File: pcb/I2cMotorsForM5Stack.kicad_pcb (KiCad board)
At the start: 2 copper layers, 60 x 50 mm, 34 parts, among them J1 FFC_connector, J2 2x15socket, J3 Conn_01x06, J4 Conn_01x06, J5 Conn_01x04, U1 TB6612FNG, U2 ATmega328PB-MU

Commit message: Rename project to I2cMotorsForM5Stack
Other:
- board text added: "I2cMotorsForM5Stack"
- board text removed: "I2CMotorsForM5Stack"
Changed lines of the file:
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@@
     (effects (font (size 1 1) (thickness 0.15)))
   )
-  (gr_text I2CMotorsForM5Stack (at 126.2988 98.5832) (layer F.SilkS)
+  (gr_text I2cMotorsForM5Stack (at 126.2988 98.5832) (layer F.SilkS)
     (effects (font (size 1.3 1.3) (thickness 0.325)))
   )
@@
     (effects (font (size 1 1) (thickness 0.15)) (justify mirror))
   )
-  (gr_text I2CMotorsForM5Stack (at 125.6988 96.5332) (layer B.SilkS)
+  (gr_text I2cMotorsForM5Stack (at 125.6988 96.5332) (layer B.SilkS)
     (effects (font (size 1.3 1.3) (thickness 0.325)) (justify mirror))
   )

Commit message: Add explanation about pads to configure address
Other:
- board text added: "Default: 0b01010010 = 0x52 = 82"
- board text added: "Pads to configure I2C slave address."
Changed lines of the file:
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@@
   (general
     (thickness 1.6)
-    (drawings 38)
+    (drawings 40)
     (tracks 593)
     (zones 0)
@@
     )
     (pad 1 np_thru_hole circle (at 0 0) (size 2.2 2.2) (drill 2.2) (layers *.Cu *.Mask))
+  )
+  (gr_text "Default: 0b01010010 = 0x52 = 82" (at 121.4238 84.6332) (layer B.SilkS)
+    (effects (font (size 1 1) (thickness 0.15)) (justify mirror))
+  )
+  (gr_text "Pads to configure I2C slave address." (at 120.8738 82.4582) (layer B.SilkS)
+    (effects (font (size 1 1) (thickness 0.15)) (justify mirror))
   )
   (gr_text GND (at 130.7488 58.2082 270) (layer F.SilkS)
@@
   (segment (start 115.1587 81.7405) (end 116.0785 80.8207) (width 0.25) (layer F.Cu) (net 46))
   (segment (start 116.0785 80.8207) (end 120.161 80.8207) (width 0.25) (layer F.Cu) (net 46))
-  (segment (start 117.9504 85.5915) (end 117.6452 85.8967) (width 0.25) (layer B.Cu) (net 58))
-  (segment (start 119.4735 84.5082) (end 118.9851 84.5082) (width 0.25) (layer F.Cu) (net 58))
-  (segment (start 118.9851 84.5082) (end 117.9504 85.5429) (width 0.25) (layer F.Cu) (net 58))
-  (segment (start 117.9504 85.5429) (end 117.9504 85.5915) (width 0.25) (layer F.Cu) (net 58))
-  (via (at 117.9504 85.5915) (size 0.8) (layers F.Cu B.Cu) (net 58))
-  (segment (start 116.4238 87.1181) (end 117.9504 85.5915) (width 0.25) (layer B.Cu) (net 58))
-  (segment (start 116.4238 92.5582) (end 116.4238 87.1181) (width 0.25) (layer B.Cu) (net 58))
   (via (at 118.1488 86.6832) (size 0.8) (drill 0.4) (layers F.Cu B.Cu) (net 47))
   (segment (start 119.4735 85.0082) (end 119.4735 85.3585) (width 0.25) (layer F.Cu) (net 47))
@@
   (segment (start 118.1488 91.7332) (end 118.9738 92.5582) (width 0.25) (layer B.Cu) (net 47))
   (segment (start 118.1488 86.6832) (end 118.1488 91.7332) (width 0.25) (layer B.Cu) (net 47))
-  (segment (start 94.4988 62.0082) (end 94.0488 62.4582) (width 1) (layer F.Cu) (net 49))
-  (segment (start 105.299 62.0082) (end 94.4988 62.0082) (width 1) (layer F.Cu) (net 49))
   (segment (start 120.161 85.6957) (end 120.0653 85.6957) (width 0.25) (layer F.Cu) (net 48))
   (segment (start 120.0653 85.6957) (end 118.8851 86.8759) (width 0.25) (layer F.Cu) (net 48))
@@
   (segment (start 121.5238 91.6079) (end 118.8851 88.9692) (width 0.25) (layer B.Cu) (net 48))
   (segment (start 121.5238 92.5582) (end 121.5238 91.6079) (width 0.25) (layer B.Cu) (net 48))
+  (segment (start 94.4988 62.0082) (end 94.0488 62.4582) (width 1) (layer F.Cu) (net 49))
+  (segment (start 105.299 62.0082) (end 94.4988 62.0082) (width 1) (layer F.Cu) (net 49))
   (segment (start 120.661 85.6957) (end 120.661 86.1841) (width 0.25) (layer F.Cu) (net 50))
   (segment (start 120.661 86.1841) (end 120.3864 86.4587) (width 0.25) (layer F.Cu) (net 50))
@@
   (segment (start 110.9485 70.568898) (end 110.02379 71.493608) (width 1) (layer F.Cu) (net 57))
   (segment (start 111.124 76.5582) (end 113.6488 76.5582) (width 1) (layer F.Cu) (net 57))
+  (segment (start 117.9504 85.5915) (end 117.6452 85.8967) (width 0.25) (layer B.Cu) (net 58))
+  (segment (start 119.4735 84.5082) (end 118.9851 84.5082) (width 0.25) (layer F.Cu) (net 58))
+  (segment (start 118.9851 84.5082) (end 117.9504 85.5429) (width 0.25) (layer F.Cu) (net 58))
+  (segment (start 117.9504 85.5429) (end 117.9504 85.5915) (width 0.25) (layer F.Cu) (net 58))
+  (via (at 117.9504 85.5915) (size 0.8) (layers F.Cu B.Cu) (net 58))
+  (segment (start 116.4238 87.1181) (end 117.9504 85.5915) (width 0.25) (layer B.Cu) (net 58))
+  (segment (start 116.4238 92.5582) (end 116.4238 87.1181) (width 0.25) (layer B.Cu) (net 58))
   (zone (net 1) (net_name GND) (layer F.Cu) (hatch edge 0.508)
     (connect_pads (clearance 0.508))

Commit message: Update something
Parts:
- removed JP3, JP4: NO, Jumper:SolderJumper-2_P1.3mm_Open_RoundedPad1.0x1.5mm
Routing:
- net Net-(JP3-Pad2): track 4.54 -> 0.00 mm
- net Net-(JP4-Pad2): track 4.42 -> 0.00 mm
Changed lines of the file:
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@@
     (thickness 1.6)
     (drawings 40)
-    (tracks 593)
+    (tracks 588)
     (zones 0)
-    (modules 34)
+    (modules 32)
     (nets 59)
   )
@@
       (rotate (xyz 0 0 0))
     )
-  )
-  (module Jumper:SolderJumper-2_P1.3mm_Open_RoundedPad1.0x1.5mm (layer F.Cu)
-    (at 128.924 81.3082 180)
-    (descr "SMD Solder Jumper, 1x1.5mm, rounded Pads, 0.3mm gap, open")
-    (tags "solder jumper open")
-    (attr virtual)
-    (fp_text reference JP4 (at 0 -1.8) (layer F.SilkS) hide
-      (effects (font (size 1 1) (thickness 0.15)))
-    )
-    (fp_text value NO (at 0 1.9) (layer F.Fab)
-      (effects (font (size 1 1) (thickness 0.15)))
-    )
-    (fp_line (start 1.65 1.25) (end -1.65 1.25) (layer F.CrtYd) (width 0.05))
-    (fp_line (start 1.65 1.25) (end 1.65 -1.25) (layer F.CrtYd) (width 0.05))
-    (fp_line (start -1.65 -1.25) (end -1.65 1.25) (layer F.CrtYd) (width 0.05))
-    (fp_line (start -1.65 -1.25) (end 1.65 -1.25) (layer F.CrtYd) (width 0.05))
-    (fp_line (start -0.7 -1) (end 0.7 -1) (layer F.SilkS) (width 0.12))
-    (fp_line (start 1.4 -0.3) (end 1.4 0.3) (layer F.SilkS) (width 0.12))
-    (fp_line (start 0.7 1) (end -0.7 1) (layer F.SilkS) (width 0.12))
-    (fp_line (start -1.4 0.3) (end -1.4 -0.3) (layer F.SilkS) (width 0.12))
-    (fp_arc (start -0.7 -0.3) (end -0.7 -1) (angle -90) (layer F.SilkS) (width 0.12))
-    (fp_arc (start -0.7 0.3) (end -1.4 0.3) (angle -90) (layer F.SilkS) (width 0.12))
-    (fp_arc (start 0.7 0.3) (end 0.7 1) (angle -90) (layer F.SilkS) (width 0.12))
-    (fp_arc (start 0.7 -0.3) (end 1.4 -0.3) (angle -90) (layer F.SilkS) (width 0.12))
-    (pad 2 smd custom (at 0.65 0 180) (size 1 0.5) (layers F.Cu F.Mask)
-      (net 56 "Net-(JP4-Pad2)") (zone_connect 2)
-      (options (clearance outline) (anchor rect))
-      (primitives
-        (gr_circle (center 0 0.25) (end 0.5 0.25) (width 0))
-        (gr_circle (center 0 -0.25) (end 0.5 -0.25) (width 0))
-        (gr_poly (pts
-           (xy 0 -0.75) (xy -0.5 -0.75) (xy -0.5 0.75) (xy 0 0.75)) (width 0))
-      ))
-    (pad 1 smd custom (at -0.65 0 180) (size 1 0.5) (layers F.Cu F.Mask)
-      (net 4 +3V3) (zone_connect 2)
-      (options (clearance outline) (anchor rect))
-      (primitives
-        (gr_circle (center 0 0.25) (end 0.5 0.25) (width 0))
-        (gr_circle (center 0 -0.25) (end 0.5 -0.25) (width 0))
-        (gr_poly (pts
-           (xy 0 -0.75) (xy 0.5 -0.75) (xy 0.5 0.75) (xy 0 0.75)) (width 0))
-      ))
-  )
-  (module Jumper:SolderJumper-2_P1.3mm_Open_RoundedPad1.0x1.5mm (layer F.Cu)
-    (at 128.924 85.4832 180)
-    (descr "SMD Solder Jumper, 1x1.5mm, rounded Pads, 0.3mm gap, open")
-    (tags "solder jumper open")
-    (attr virtual)
-    (fp_text reference JP3 (at 0 -1.8) (layer F.SilkS) hide
-      (effects (font (size 1 1) (thickness 0.15)))
-    )
-    (fp_text value NO (at 0 1.9) (layer F.Fab)
-      (effects (font (size 1 1) (thickness 0.15)))
-    )
-    (fp_line (start 1.65 1.25) (end -1.65 1.25) (layer F.CrtYd) (width 0.05))
-    (fp_line (start 1.65 1.25) (end 1.65 -1.25) (layer F.CrtYd) (width 0.05))
-    (fp_line (start -1.65 -1.25) (end -1.65 1.25) (layer F.CrtYd) (width 0.05))
-    (fp_line (start -1.65 -1.25) (end 1.65 -1.25) (layer F.CrtYd) (width 0.05))
-    (fp_line (start -0.7 -1) (end 0.7 -1) (layer F.SilkS) (width 0.12))
-    (fp_line (start 1.4 -0.3) (end 1.4 0.3) (layer F.SilkS) (width 0.12))
-    (fp_line (start 0.7 1) (end -0.7 1) (layer F.SilkS) (width 0.12))
-    (fp_line (start -1.4 0.3) (end -1.4 -0.3) (layer F.SilkS) (width 0.12))
-    (fp_arc (start -0.7 -0.3) (end -0.7 -1) (angle -90) (layer F.SilkS) (width 0.12))
-    (fp_arc (start -0.7 0.3) (end -1.4 0.3) (angle -90) (layer F.SilkS) (width 0.12))
-    (fp_arc (start 0.7 0.3) (end 0.7 1) (angle -90) (layer F.SilkS) (width 0.12))
-    (fp_arc (start 0.7 -0.3) (end 1.4 -0.3) (angle -90) (layer F.SilkS) (width 0.12))
-    (pad 2 smd custom (at 0.65 0 180) (size 1 0.5) (layers F.Cu F.Mask)
-      (net 55 "Net-(JP3-Pad2)") (zone_connect 2)
-      (options (clearance outline) (anchor rect))
-      (primitives
-        (gr_circle (center 0 0.25) (end 0.5 0.25) (width 0))
-        (gr_circle (center 0 -0.25) (end 0.5 -0.25) (width 0))
-        (gr_poly (pts
-           (xy 0 -0.75) (xy -0.5 -0.75) (xy -0.5 0.75) (xy 0 0.75)) (width 0))
-      ))
-    (pad 1 smd custom (at -0.65 0 180) (size 1 0.5) (layers F.Cu F.Mask)
-      (net 1 GND) (zone_connect 2)
-      (options (clearance outline) (anchor rect))
-      (primitives
-        (gr_circle (center 0 0.25) (end 0.5 0.25) (width 0))
-        (gr_circle (center 0 -0.25) (end 0.5 -0.25) (width 0))
-        (gr_poly (pts
-           (xy 0 -0.75) (xy 0.5 -0.75) (xy 0.5 0.75) (xy 0 0.75)) (width 0))
-      ))
   )
   (module footprints:2x03_P2.54mm_Pads (layer F.Cu)
@@
   (segment (start 129.3157 87.7251) (end 127.5191 87.7251) (width 0.25) (layer B.Cu) (net 54))
   (segment (start 134.1488 92.5582) (end 129.3157 87.7251) (width 0.25) (layer B.Cu) (net 54))
-  (segment (start 128.274 85.4832) (end 126.799 84.0082) (width 0.25) (layer F.Cu) (net 55))
-  (segment (start 126.799 84.0082) (end 124.3485 84.0082) (width 0.25) (layer F.Cu) (net 55))
-  (segment (start 128.274 81.3082) (end 127.0559 81.3082) (width 0.25) (layer F.Cu) (net 56))
-  (segment (start 127.0559 81.3082) (end 125.8559 82.5082) (width 0.25) (layer F.Cu) (net 56))
-  (segment (start 125.8559 82.5082) (end 124.3485 82.5082) (width 0.25) (layer F.Cu) (net 56))
   (segment (start 112.6489 76.8082) (end 112.2859 76.8082) (width 0.25) (layer F.Cu) (net 57))
   (segment (start 112.2859 76.8082) (end 112.0487 76.571) (width 0.25) (layer F.Cu) (net 57))

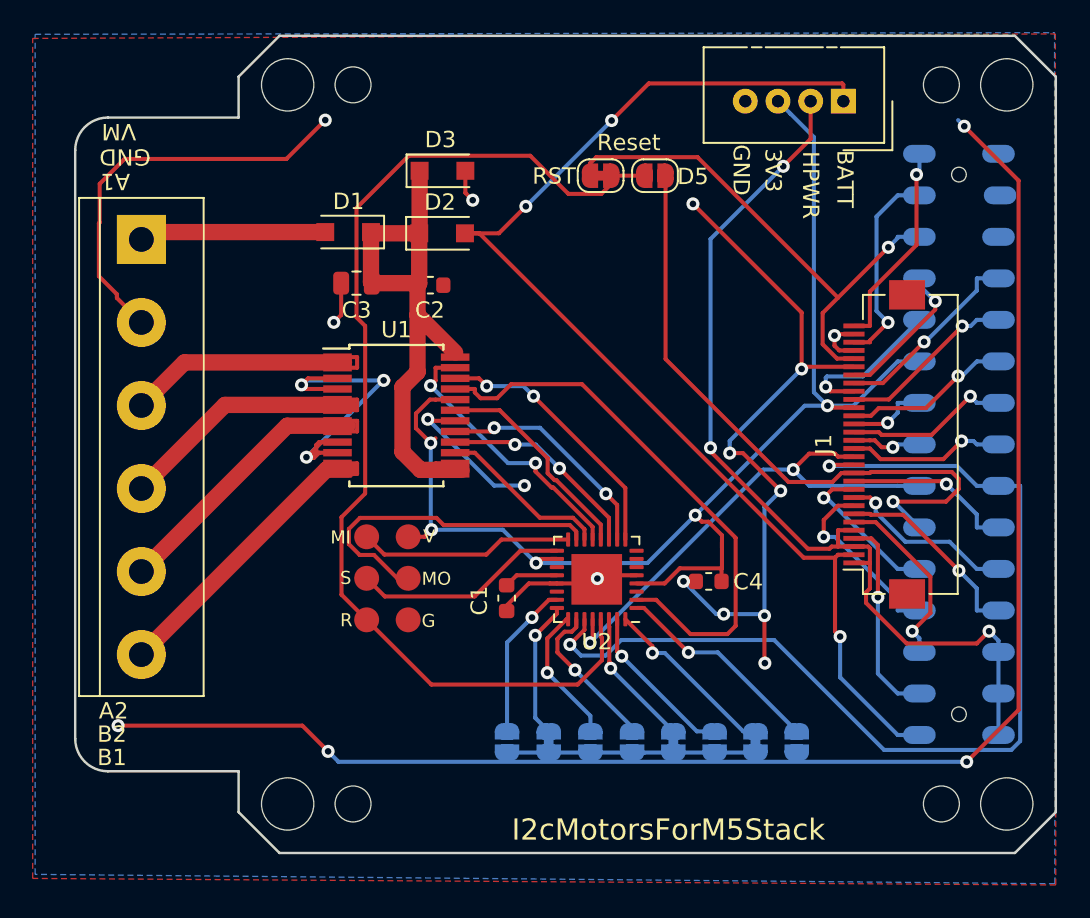
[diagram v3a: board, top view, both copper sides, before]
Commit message: Separate HPWR to NC0-2 for Core2
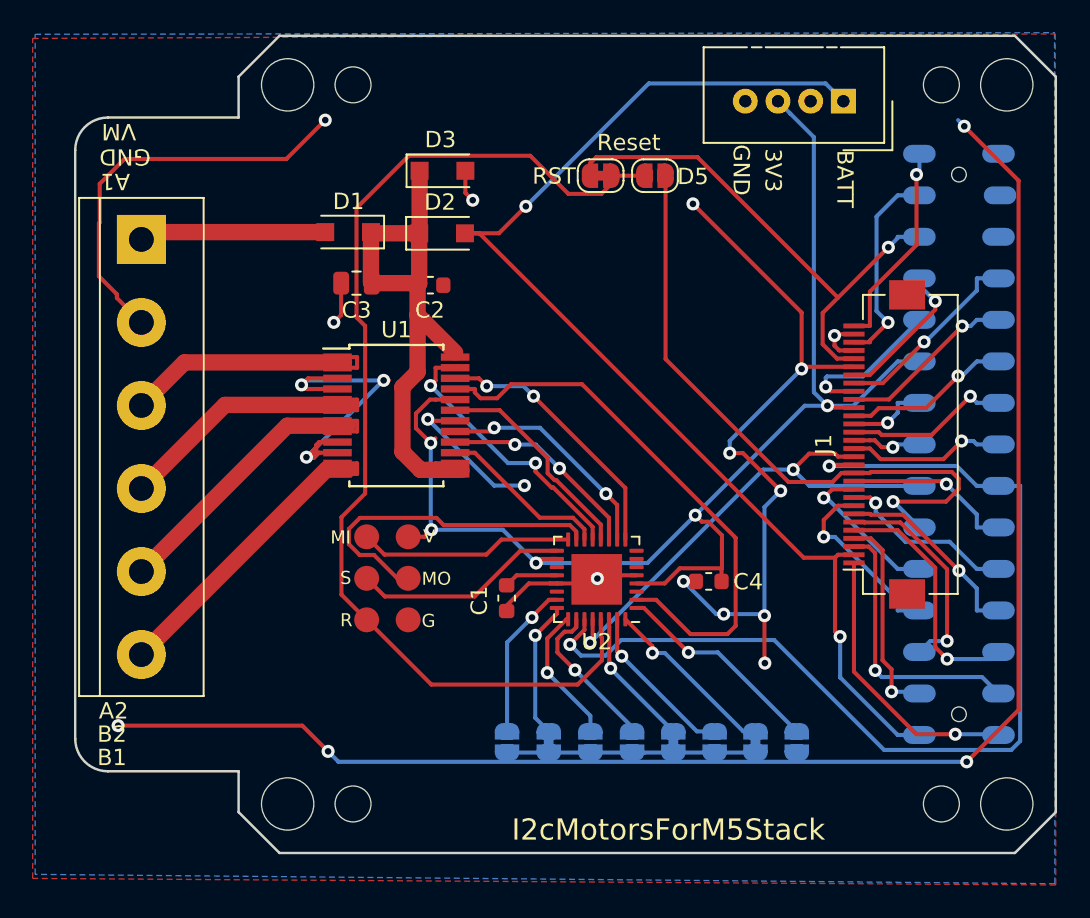
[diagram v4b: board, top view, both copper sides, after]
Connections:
- J1 pad 1: /HPWR -> /NC2
- J1 pad 3: /HPWR -> /NC1
- J1 pad 5: /HPWR -> /NC0
- J2 pad 26: /HPWR -> /NC0
- J2 pad 28: /HPWR -> /NC1
- J2 pad 30: /HPWR -> /NC2
- J5 pad 2: /HPWR -> Net-(J5-Pad2)
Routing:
- net /HPWR: track 58.1 -> 0.00 mm, vias 3 -> 0
- net /NC2: track 0.00 -> 17.1 mm, vias 0 -> 1
- net /NC1: track 0.00 -> 16.8 mm, vias 0 -> 1
- net /NC0: track 0.00 -> 15.1 mm, vias 0 -> 1
- net /34: track 11.3 -> 13.3 mm
- net +BATT: track 73.9 -> 73.3 mm, vias 3 -> 2
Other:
- board text added: "Rev2020.09"
- board text removed: "HPWR"
- board text removed: "Rev2020.05"
